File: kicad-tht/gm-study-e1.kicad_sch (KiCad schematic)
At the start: 12 parts

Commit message: file updates
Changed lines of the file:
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@@
   (symbol (lib_id "Device:R_Small") (at 69.85 179.07 90) (unit 1)
     (in_bom yes) (on_board yes)
-    (property "Reference" "R29" (id 0) (at 69.85 176.53 90))
-    (property "Value" "160" (id 1) (at 69.85 181.61 90))
+    (property "Reference" "R29" (id 0) (at 64.77 177.8 90))
+    (property "Value" "160" (id 1) (at 74.93 177.8 90))
     (property "Footprint" "Resistor_SMD:R_0402_1005Metric" (id 2) (at 69.85 179.07 0)
       (effects (font (size 1.27 1.27)) hide)
@@
     )
     (path "/55aa19aa-4e00-4e71-83a9-51c462d9a2c0/aea87dd1-9dac-4bcb-9ac9-50c43158bf69"
-      (reference "BZ1") (unit 1) (value "Buzzer") (footprint "Buzzer_Beeper:Buzzer_Murata_PKLCS1212E")
+      (reference "BZ1") (unit 1) (value "Buzzer") (footprint "FM4DD:Buzzer_Murata_PKLCS1212E")
     )
     (path "/55aa19aa-4e00-4e71-83a9-51c462d9a2c0/08d6b081-ef12-4fdd-8482-faa056642ae9"
@@
       (reference "J1") (unit 1) (value "Conn_01x16") (footprint "Connector_PinHeader_2.54mm:PinHeader_1x16_P2.54mm_Vertical")
     )
-    (path "/c2ce2db8-0c6b-4dd5-bb07-3b39fea01243/cdd55ec0-a32d-4e52-b010-c9945ae875a9"
-      (reference "JP1") (unit 1) (value "Jumper") (footprint "Connector_PinHeader_2.54mm:PinHeader_1x02_P2.54mm_Vertical")
-    )
     (path "/55aa19aa-4e00-4e71-83a9-51c462d9a2c0/f9f2c2ff-1c55-49dc-9160-b1239897bb85"
       (reference "L1") (unit 1) (value "4.7uH") (footprint "Inductor_SMD:L_0603_1608Metric")
@@
     )
     (path "/c2ce2db8-0c6b-4dd5-bb07-3b39fea01243/af96fff0-3375-4c10-bbb9-2b61a3c51e30"
-      (reference "R1") (unit 1) (value "10K") (footprint "Resistor_SMD:R_0402_1005Metric")
+      (reference "R1") (unit 1) (value "100K") (footprint "Resistor_SMD:R_0402_1005Metric")
     )
     (path "/c2ce2db8-0c6b-4dd5-bb07-3b39fea01243/05a95282-20a4-430c-9cca-91e2a5af233e"
-      (reference "R2") (unit 1) (value "10K") (footprint "Resistor_SMD:R_0402_1005Metric")
+      (reference "R2") (unit 1) (value "100K") (footprint "Resistor_SMD:R_0402_1005Metric")
     )
     (path "/c2ce2db8-0c6b-4dd5-bb07-3b39fea01243/cf37650b-0af1-4e22-a75c-302588045384"
-      (reference "R3") (unit 1) (value "10K") (footprint "Resistor_SMD:R_0402_1005Metric")
+      (reference "R3") (unit 1) (value "100K") (footprint "Resistor_SMD:R_0402_1005Metric")
     )
     (path "/c2ce2db8-0c6b-4dd5-bb07-3b39fea01243/fcde6358-da36-4fc6-8a2c-ddd9fd14425c"
-      (reference "R4") (unit 1) (value "10K") (footprint "Resistor_SMD:R_0402_1005Metric")
+      (reference "R4") (unit 1) (value "100K") (footprint "Resistor_SMD:R_0402_1005Metric")
     )
     (path "/c2ce2db8-0c6b-4dd5-bb07-3b39fea01243/523a206e-813b-466f-9258-27b6613d5417"
-      (reference "R5") (unit 1) (value "10K") (footprint "Resistor_SMD:R_0402_1005Metric")
+      (reference "R5") (unit 1) (value "100K") (footprint "Resistor_SMD:R_0402_1005Metric")
     )
     (path "/c2ce2db8-0c6b-4dd5-bb07-3b39fea01243/95f58958-d920-4ce0-9313-4f6e5f0aa077"
-      (reference "R6") (unit 1) (value "10K") (footprint "Resistor_SMD:R_0402_1005Metric")
+      (reference "R6") (unit 1) (value "100K") (footprint "Resistor_SMD:R_0402_1005Metric")
     )
     (path "/c2ce2db8-0c6b-4dd5-bb07-3b39fea01243/fc4ff3b0-9312-4e40-b230-cc54a1976deb"
-      (reference "R7") (unit 1) (value "10K") (footprint "Resistor_SMD:R_0402_1005Metric")
+      (reference "R7") (unit 1) (value "100K") (footprint "Resistor_SMD:R_0402_1005Metric")
     )
     (path "/c2ce2db8-0c6b-4dd5-bb07-3b39fea01243/68048d45-bbc7-43be-b391-1e28da99b42c"
-      (reference "R8") (unit 1) (value "10K") (footprint "Resistor_SMD:R_0402_1005Metric")
+      (reference "R8") (unit 1) (value "100K") (footprint "Resistor_SMD:R_0402_1005Metric")
     )
     (path "/c2ce2db8-0c6b-4dd5-bb07-3b39fea01243/85e65d40-dcdc-4cc8-baea-9e34c493f165"
-      (reference "R9") (unit 1) (value "10K") (footprint "Resistor_SMD:R_0402_1005Metric")
+      (reference "R9") (unit 1) (value "100K") (footprint "Resistor_SMD:R_0402_1005Metric")
     )
     (path "/c2ce2db8-0c6b-4dd5-bb07-3b39fea01243/67899650-a90f-4aa9-b7e4-545bab6b4744"
-      (reference "R10") (unit 1) (value "10K") (footprint "Resistor_SMD:R_0402_1005Metric")
+      (reference "R10") (unit 1) (value "100K") (footprint "Resistor_SMD:R_0402_1005Metric")
     )
     (path "/55aa19aa-4e00-4e71-83a9-51c462d9a2c0/99f089fa-5203-42f4-bc84-a57394ca1da4"
-      (reference "R11") (unit 1) (value "160") (footprint "Resistor_SMD:R_0402_1005Metric")
+      (reference "R11") (unit 1) (value "200") (footprint "Resistor_SMD:R_0402_1005Metric")
     )
     (path "/55aa19aa-4e00-4e71-83a9-51c462d9a2c0/387ac8c6-0d9a-4f7a-89c9-2f3d22ae6a2f"
-      (reference "R12") (unit 1) (value "160") (footprint "Resistor_SMD:R_0402_1005Metric")
+      (reference "R12") (unit 1) (value "200") (footprint "Resistor_SMD:R_0402_1005Metric")
     )
     (path "/55aa19aa-4e00-4e71-83a9-51c462d9a2c0/b07b1386-8d41-496d-b474-bc3b02454877"
-      (reference "R13") (unit 1) (value "160") (footprint "Resistor_SMD:R_0402_1005Metric")
+      (reference "R13") (unit 1) (value "200") (footprint "Resistor_SMD:R_0402_1005Metric")
     )
     (path "/55aa19aa-4e00-4e71-83a9-51c462d9a2c0/a6ea8723-6c9a-4e69-92a4-16d4b0a51c42"
-      (reference "R14") (unit 1) (value "160") (footprint "Resistor_SMD:R_0402_1005Metric")
+      (reference "R14") (unit 1) (value "200") (footprint "Resistor_SMD:R_0402_1005Metric")
     )
     (path "/55aa19aa-4e00-4e71-83a9-51c462d9a2c0/6d485ad6-ed5e-4b11-8f40-020df7b546af"
-      (reference "R15") (unit 1) (value "160") (footprint "Resistor_SMD:R_0402_1005Metric")
+      (reference "R15") (unit 1) (value "200") (footprint "Resistor_SMD:R_0402_1005Metric")
     )
     (path "/55aa19aa-4e00-4e71-83a9-51c462d9a2c0/a3d7eaec-ebf2-4474-bf7f-990caeb3ca18"
-      (reference "R16") (unit 1) (value "160") (footprint "Resistor_SMD:R_0402_1005Metric")
+      (reference "R16") (unit 1) (value "200") (footprint "Resistor_SMD:R_0402_1005Metric")
     )
     (path "/55aa19aa-4e00-4e71-83a9-51c462d9a2c0/6056104d-d3e9-4af8-bd93-bcd9d898d970"
-      (reference "R17") (unit 1) (value "160") (footprint "Resistor_SMD:R_0402_1005Metric")
+      (reference "R17") (unit 1) (value "200") (footprint "Resistor_SMD:R_0402_1005Metric")
     )
     (path "/55aa19aa-4e00-4e71-83a9-51c462d9a2c0/c9b1dbe6-92df-42ce-8804-c4378d3ae055"
-      (reference "R18") (unit 1) (value "160") (footprint "Resistor_SMD:R_0402_1005Metric")
+      (reference "R18") (unit 1) (value "200") (footprint "Resistor_SMD:R_0402_1005Metric")
     )
     (path "/55aa19aa-4e00-4e71-83a9-51c462d9a2c0/226598e4-efa8-428b-9a17-6d7b750837c2"
-      (reference "R19") (unit 1) (value "160") (footprint "Resistor_SMD:R_0402_1005Metric")
+      (reference "R19") (unit 1) (value "200") (footprint "Resistor_SMD:R_0402_1005Metric")
     )
     (path "/55aa19aa-4e00-4e71-83a9-51c462d9a2c0/fcf81bc3-fa75-43a3-ae0a-d6dad0120be0"
-      (reference "R20") (unit 1) (value "160") (footprint "Resistor_SMD:R_0402_1005Metric")
+      (reference "R20") (unit 1) (value "200") (footprint "Resistor_SMD:R_0402_1005Metric")
     )
     (path "/c2ce2db8-0c6b-4dd5-bb07-3b39fea01243/a17e37ea-ea68-46af-adf7-a4b8b99a41a3"
@@
     )
     (path "/55aa19aa-4e00-4e71-83a9-51c462d9a2c0/c642ed85-95b4-496b-b07e-89d16238bb9e"
-      (reference "R30") (unit 1) (value "160") (footprint "Resistor_THT:R_Axial_DIN0204_L3.6mm_D1.6mm_P5.08mm_Horizontal")
+      (reference "R30") (unit 1) (value "100") (footprint "Resistor_THT:R_Axial_DIN0204_L3.6mm_D1.6mm_P5.08mm_Horizontal")
     )
     (path "/55aa19aa-4e00-4e71-83a9-51c462d9a2c0/0d340f53-7f13-4000-9a47-40d819c1f061"

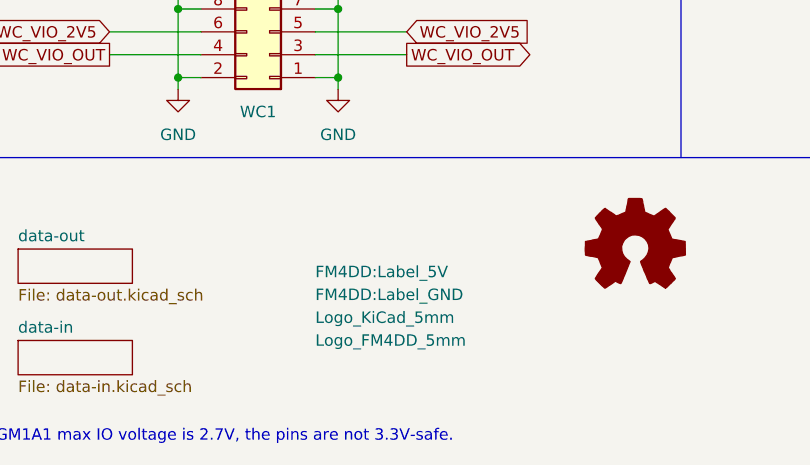
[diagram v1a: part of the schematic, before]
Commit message: New THT PCB v1.1 updates J1 level translation IC
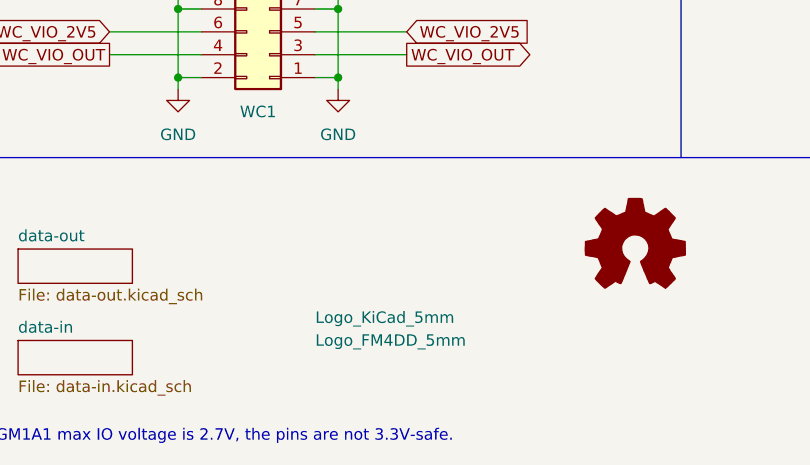
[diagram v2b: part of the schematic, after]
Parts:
- LED10: footprint FM4DD:LED_0402_FPGA -> FM4DD:LED_0402_no_frame
